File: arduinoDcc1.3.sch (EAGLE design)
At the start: 33 parts, among them IC1 7812TV, T2 2N2222, X1 MKDSN1,5/3-5,08, X2 MKDSN1,5/2-5,08, X3 MKDSN1,5/2-5,08, X4 MKDSN1,5/2-5,08, X5 MKDSN1,5/2-5,08, X6 MKDSN1,5/2-5,08, X7 MKDSN1,5/2-5,08, X8 MKDSN1,5/2-5,08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

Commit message: change voltage regulator to swtiching power supply
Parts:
- C1: value 220 uF -> 330 uF
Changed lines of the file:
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@@
 <part name="B1" library="rectifier" deviceset="RB1A" device=""/>
 <part name="GND1" library="supply1" deviceset="GND" device=""/>
-<part name="C1" library="SparkFun-Capacitors" deviceset="CAP_POL" device="PTH1" value="220 uF"/>
+<part name="C1" library="SparkFun-Capacitors" deviceset="CAP_POL" device="PTH1" value="330 uF"/>
 <part name="SPARK-0102" library="SparkFun-Electromechanical" deviceset="SWITCH-SPDT" device="PTH"/>
 <part name="LED1" library="SparkFun-LED" deviceset="LED" device="3MM"/>

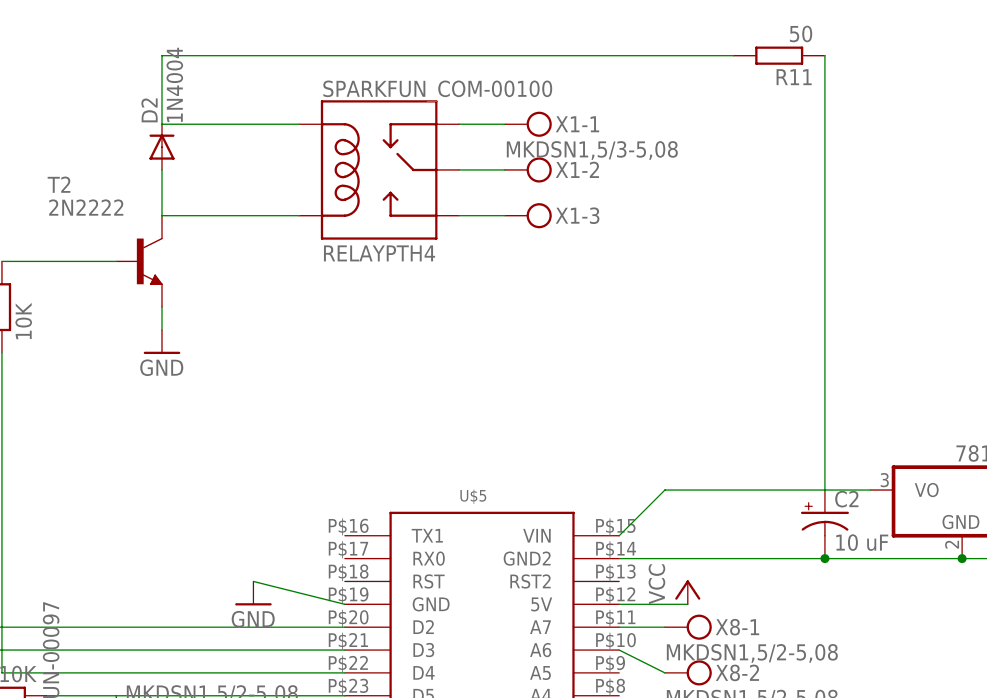
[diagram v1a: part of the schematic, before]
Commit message: new version 1.3, with DC-DC converter instead of voltage regulator
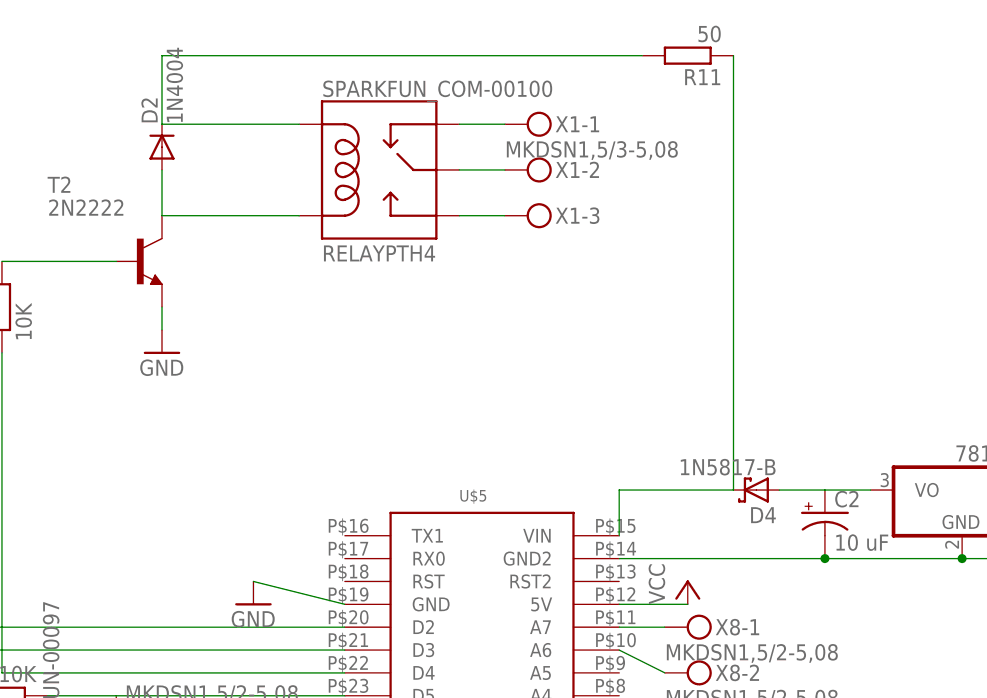
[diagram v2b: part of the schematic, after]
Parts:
- added D4: 1N5817-B, diode:1N5817-B
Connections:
- new net N$31: D4.C, R11.1, U$5.VIN
- net N$28: now also D4.A; no longer R11.1, U$5.VIN
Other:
- moved on the sheet: R11
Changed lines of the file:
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@@
 <part name="R6" library="eagle-ltspice" deviceset="R" device="0207/10" value="400"/>
 <part name="R7" library="eagle-ltspice" deviceset="R" device="0207/10" value="400"/>
+<part name="D4" library="diode" deviceset="1N581*" device="" technology="7-B"/>
 </parts>
 <sheets>
@@
 <instance part="IC1" gate="A1" x="218.44" y="53.34" rot="MR0"/>
 <instance part="R8" gate="G$1" x="111.76" y="73.66" rot="R90"/>
-<instance part="R11" gate="G$1" x="198.12" y="101.6" rot="R180"/>
+<instance part="R11" gate="G$1" x="187.96" y="101.6" rot="R180"/>
 <instance part="R5" gate="G$1" x="165.1" y="2.54" rot="R180"/>
 <instance part="R6" gate="G$1" x="162.56" y="-15.24" rot="R180"/>
 <instance part="R7" gate="G$1" x="160.02" y="-27.94" rot="R180"/>
+<instance part="D4" gate="G$1" x="195.58" y="53.34" rot="R180"/>
 </instances>
 <busses>
@@
 </segment>
 </net>
-<net name="N$28" class="0">
-<segment>
-<pinref part="U$5" gate="G$1" pin="VIN"/>
-<pinref part="C2" gate="G$1" pin="+"/>
-<wire x1="180.34" y1="48.26" x2="185.42" y2="53.34" width="0.1524" layer="91"/>
-<wire x1="185.42" y1="53.34" x2="203.2" y2="53.34" width="0.1524" layer="91"/>
-<pinref part="IC1" gate="A1" pin="VO"/>
-<wire x1="208.28" y1="53.34" x2="203.2" y2="53.34" width="0.1524" layer="91"/>
-<pinref part="R11" gate="G$1" pin="1"/>
-<wire x1="203.2" y1="101.6" x2="203.2" y2="53.34" width="0.1524" layer="91"/>
-</segment>
-</net>
 <net name="N$14" class="0">
 <segment>
@@
 <wire x1="129.54" y1="101.6" x2="129.54" y2="93.98" width="0.1524" layer="91"/>
 <pinref part="R11" gate="G$1" pin="2"/>
-<wire x1="129.54" y1="101.6" x2="193.04" y2="101.6" width="0.1524" layer="91"/>
-</segment>
-</net>
+<wire x1="129.54" y1="101.6" x2="182.88" y2="101.6" width="0.1524" layer="91"/>
+</segment>
+</net>
+<net name="N$31" class="0">
+<segment>
+<pinref part="D4" gate="G$1" pin="C"/>
+<pinref part="R11" gate="G$1" pin="1"/>
+<wire x1="193.04" y1="101.6" x2="193.04" y2="53.34" width="0.1524" layer="91"/>
+<wire x1="193.04" y1="53.34" x2="180.34" y2="53.34" width="0.1524" layer="91"/>
+<pinref part="U$5" gate="G$1" pin="VIN"/>
+<wire x1="180.34" y1="53.34" x2="180.34" y2="48.26" width="0.1524" layer="91"/>
+</segment>
+</net>
+<net name="N$28" class="0">
+<segment>
+<pinref part="IC1" gate="A1" pin="VO"/>
+<pinref part="C2" gate="G$1" pin="+"/>
+<wire x1="208.28" y1="53.34" x2="203.2" y2="53.34" width="0.1524" layer="91"/>
+<pinref part="D4" gate="G$1" pin="A"/>
+<wire x1="203.2" y1="53.34" x2="198.12" y2="53.34" width="0.1524" layer="91"/>
+</segment>
+</net>
